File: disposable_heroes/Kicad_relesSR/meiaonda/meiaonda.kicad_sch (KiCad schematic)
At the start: 44 parts, among them J1 Canal 1 - V_{in}, J10 Gerador Sinal, J2 Fonte 12V, J3 Fonte 5V - VB, J4 GPIO22, J5 GPIO26, J6 GPIO6, J7 GPIO13, J8 GPIO27, J9 Canal 2 - V_{out}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

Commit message: problemas com o onda completa
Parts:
- renumbered K13 to K10, K14 to K11
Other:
- moved on the sheet: C5, C6, K10, K11, R3, R4

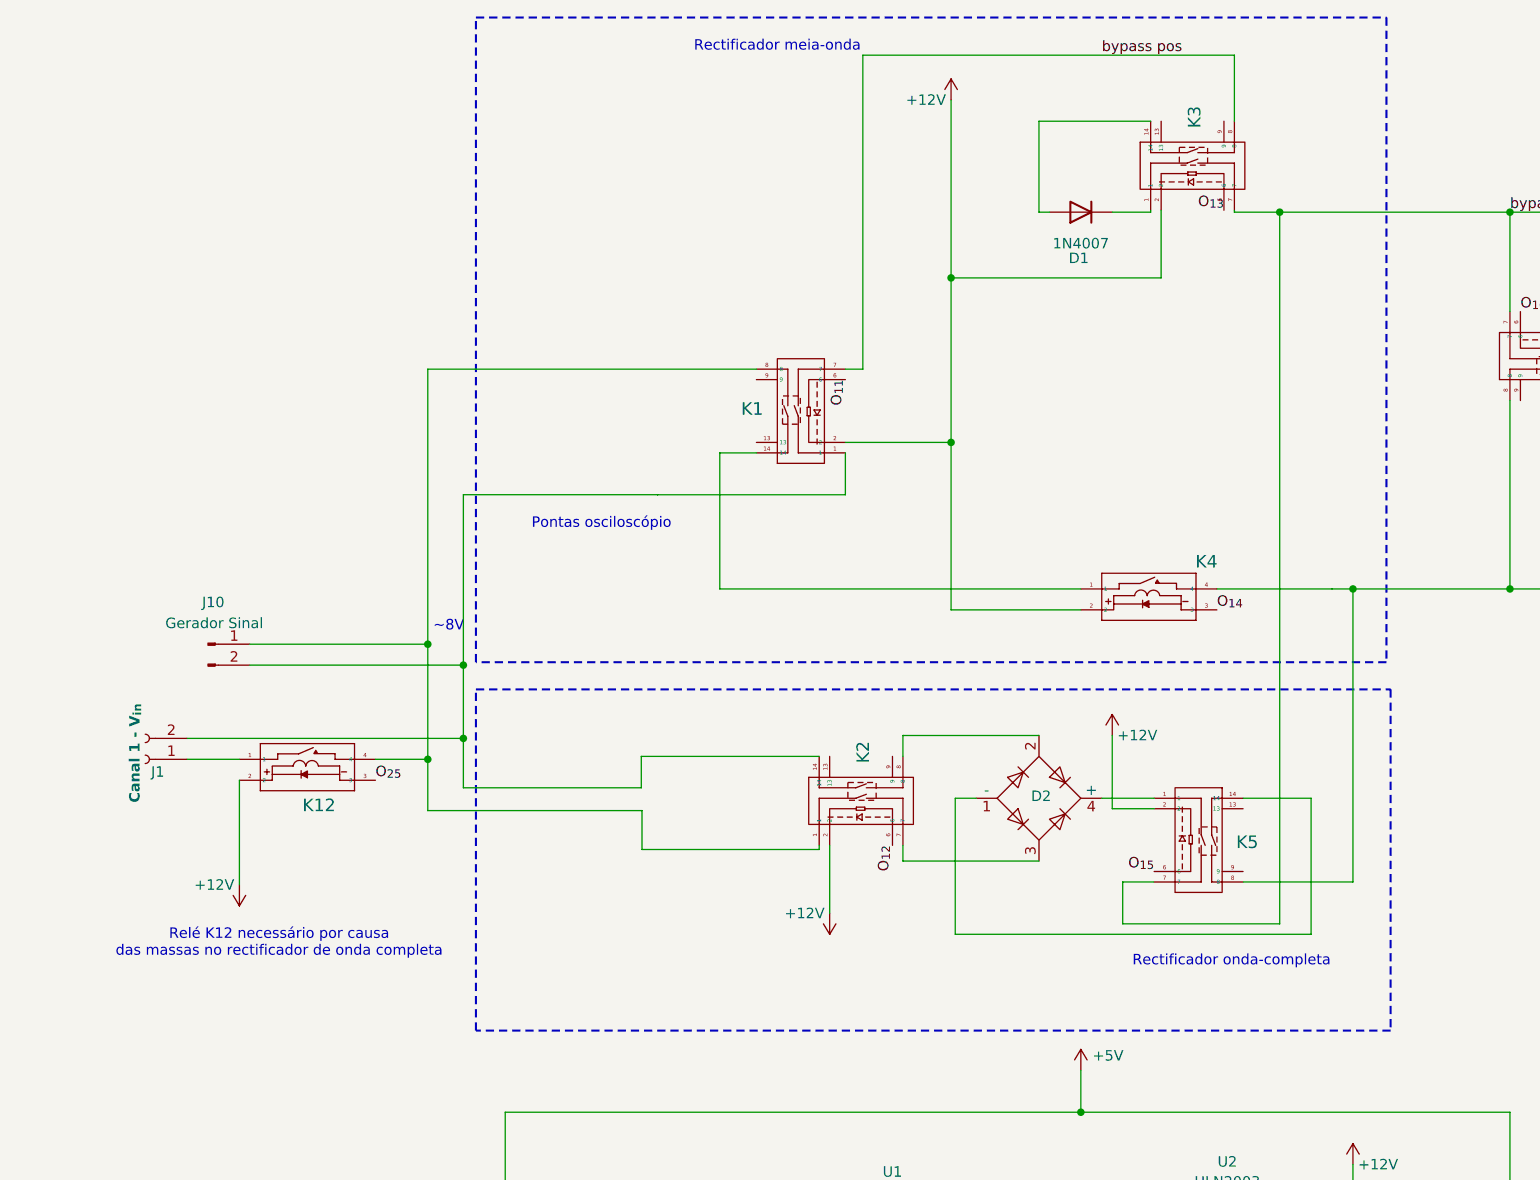
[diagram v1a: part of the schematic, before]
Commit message: Rectificador de onda completa a funcionar, somente com o canal 1 ligado à saída, aparentemente, não funciona só com o canal 2
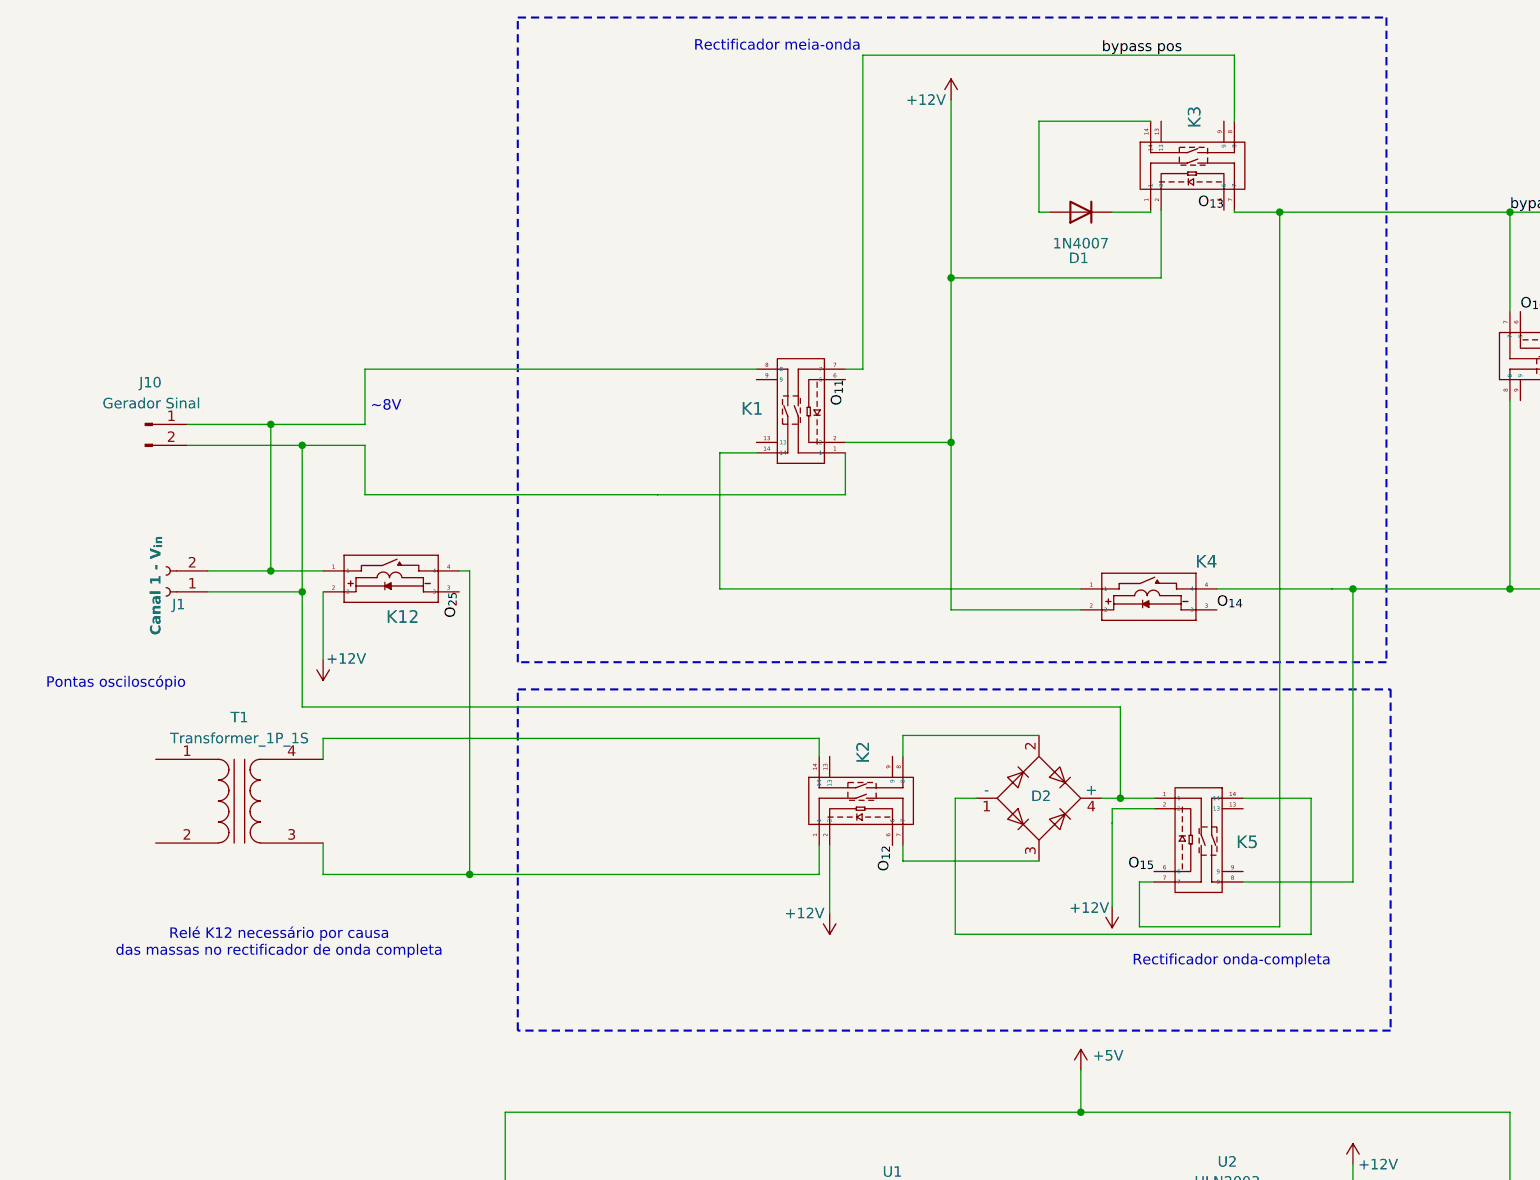
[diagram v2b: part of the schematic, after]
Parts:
- added T1: Transformer_1P_1S, symbol Device:Transformer_1P_1S
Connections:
- net at D2.4 (+), K5.1: now also J1.1 (Pin_1), J10.2 (Pin_2), K1.1
- net at J10.1 (Pin_1), K1.8: now also J1.2 (Pin_2), K12.1; no longer K12.4, K2.1
- new net: K12.4, K2.1, T1.3 (SA)
- new net: K2.14, T1.4 (SB)
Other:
- moved on the sheet: J1, J10, K12

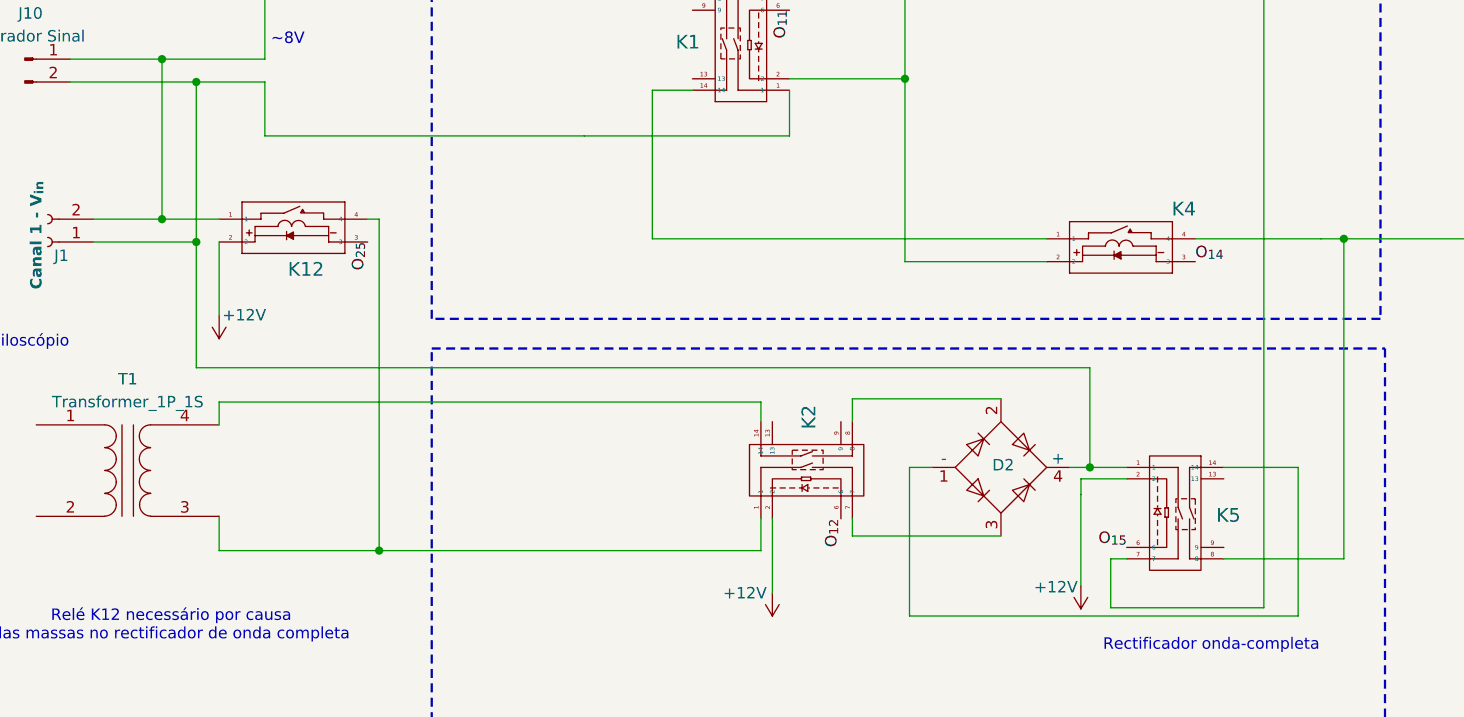
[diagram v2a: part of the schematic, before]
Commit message: adiocionado relé K13, para cortar o sinal para a meia onda
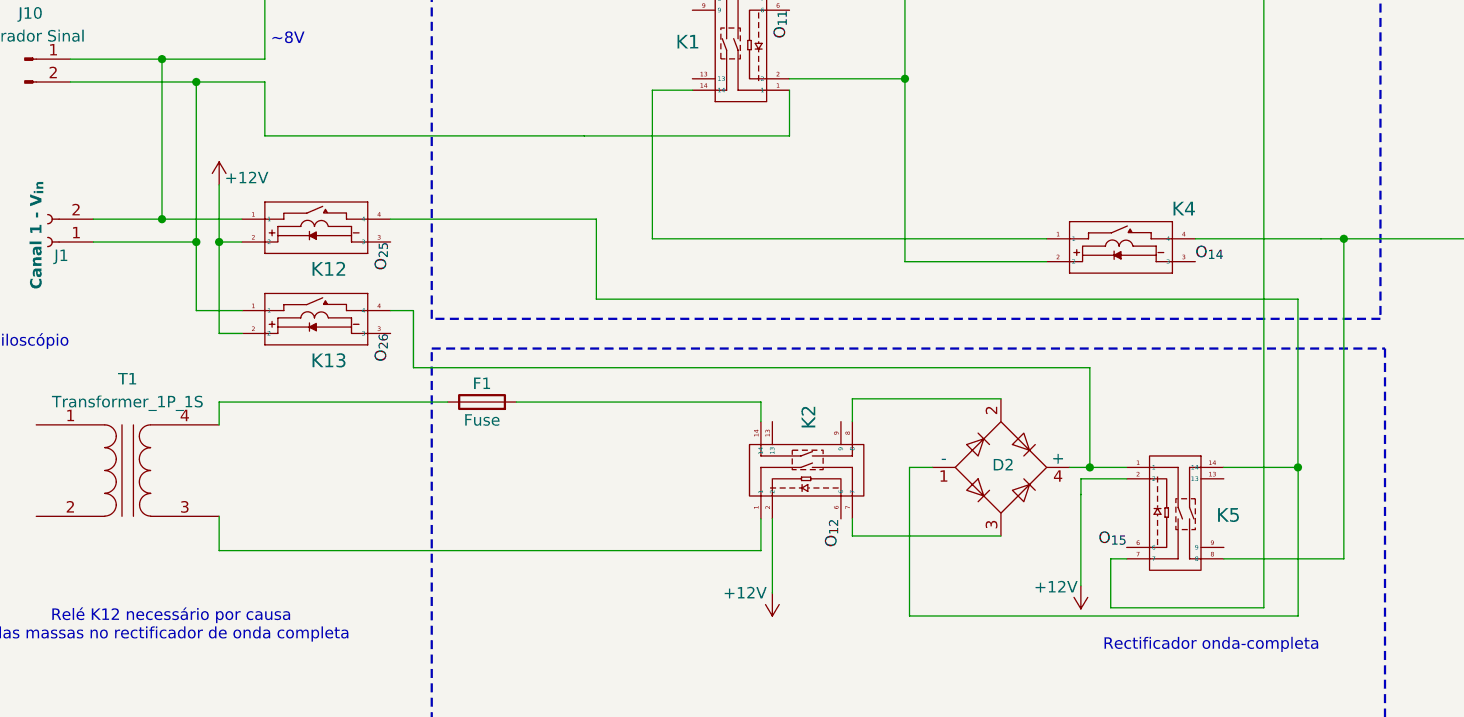
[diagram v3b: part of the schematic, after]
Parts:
- added F1: Fuse, symbol Device:Fuse
- added K13: 3570-1331-123, 3570-1331-123:SIP_3570-1331_COM, symbol 3570-1331-123:3570-1331-123
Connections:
- net +12V: now also K13.2
- net at D2.1 (-), K5.14: now also K12.4
- net at J1.1 (Pin_1), J10.2 (Pin_2), K1.1: now also K13.1; no longer D2.4 (+), K5.1
- net at K2.1, T1.3 (SA): no longer K12.4
- net at K2.14: now also F1.2; no longer T1.4 (SB)
- new net: D2.4 (+), K13.4, K5.1
- new net: F1.1, T1.4 (SB)
- new net O_{26}: K13.3
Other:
- moved on the sheet: K12

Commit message: minor update kicad
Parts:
- removed C5: 10uF, Capacitor_THT:CP_Radial_D6.3mm_P2.50mm, symbol Device:C_Polarized
- removed K10, K11: 3572-1220-123, 3572-1220-123:RELAY8_3572-1220-053_COM, symbol 3572-1220-123:3572-1220-123
- removed R3: 1K, Resistor_THT:R_Axial_DIN0207_L6.3mm_D2.5mm_P15.24mm_Horizontal, symbol Device:R
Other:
- note added: "8 relés duplos 5 relé simples"
- note removed: "8 relés duplos 1 relé simples"
- note removed: "Reles duplos"

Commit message: update kicad
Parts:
- removed J3: Fonte 5V - VB, Connector_PinHeader_2.54mm:PinHeader_1x02_P2.54mm_Vertical, symbol Connector:Conn_01x02_Pin
- removed T1: Transformer_1P_1S, symbol Device:Transformer_1P_1S
- added C_{Out}1: 1uF, Capacitor_THT:CP_Radial_D5.0mm_P2.00mm, symbol Device:C_Polarized
- added C_{adj}1: 10uF, Capacitor_THT:CP_Radial_D5.0mm_P2.00mm, symbol Device:C
- added C_{i}1: 100nF, Capacitor_THT:C_Disc_D5.1mm_W3.2mm_P5.00mm, symbol Device:C
- added D3, D4: 1N4007, Diode_THT:D_DO-41_SOD81_P10.16mm_Horizontal, symbol Diode:1N4007
- added J12: V_{in}, Connector_PinHeader_2.54mm:PinHeader_1x01_P2.54mm_Vertical, symbol Connector:Conn_01x01_Pin
- added J13: V_{out}, Connector_PinHeader_2.54mm:PinHeader_1x05_P2.54mm_Vertical, symbol Connector:Conn_01x05_Pin
- added R4: 330, Resistor_THT:R_Axial_DIN0207_L6.3mm_D2.5mm_P15.24mm_Horizontal, symbol Device:R
- added R5: 1K, Resistor_THT:R_Axial_DIN0207_L6.3mm_D2.5mm_P15.24mm_Horizontal, symbol Device:R
- added U5: LM317_TO-220, Package_TO_SOT_THT:TO-220-3_Vertical, symbol Regulator_Linear:LM317_TO-220
- C6: footprint Capacitor_THT:CP_Radial_D6.3mm_P2.50mm -> Capacitor_THT:CP_Radial_D5.0mm_P2.00mm
- F1: footprint (none) -> Fuse:Fuseholder_Cylinder-5x20mm_Stelvio-Kontek_PTF78_Horizontal_Open
- J2: value Fonte 12V -> Transformer
- renumbered R4 to R3
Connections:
- net +12V: no longer J2.1 (Pin_1)
- net GND: now also C_{Out}1.2, C_{adj}1.2, C_{i}1.2, R5.2; no longer J2.2 (Pin_2)
- net I_{26}: now also U3.4 (Q4)
- net O_{26}: now also U4.11 (O6)
- net at K2.1: now also J2.2 (Pin_2)
- net at F1.1: now also J2.1 (Pin_1)
- new net: C_{Out}1.1, D3.2 (A), D4.1 (K), J13.1 (Pin_1), J13.2 (Pin_2), J13.3 (Pin_3), J13.4 (Pin_4), J13.5 (Pin_5), R4.1, U5.2 (VO)
- new net: C_{adj}1.1, D4.2 (A), R4.2, R5.1, U5.1 (ADJ)
- new net: C_{i}1.1, D3.1 (K), J12.1 (Pin_1), U5.3 (VI)
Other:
- note added: "12V vindos do VirtualBench"
- note added: "5V que alimenta os CI"
- moved on the sheet: C3, C4, C6, H1, H2, H3, H4, J4, J5, J6, J7, J8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
